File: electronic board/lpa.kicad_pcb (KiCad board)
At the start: 2 copper layers, 143 x 74 mm, 81 parts, among them CON1 BARREL_JACK, IC1 ATMEGA328-A, P2 CONN_3X2, U1 SD_CARD, U2 AP1509, U3 TLC5941, U4 TLC5941, U5 TLC5941, X1 CRYSTAL_SMD

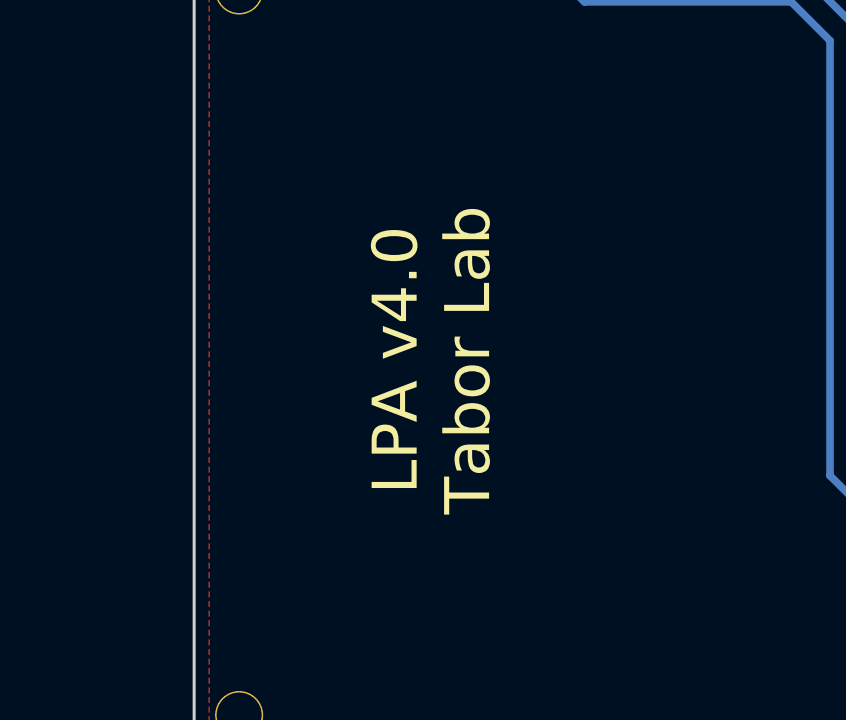
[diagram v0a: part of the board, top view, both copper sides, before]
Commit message: Updated LPA version in board silkscreen.
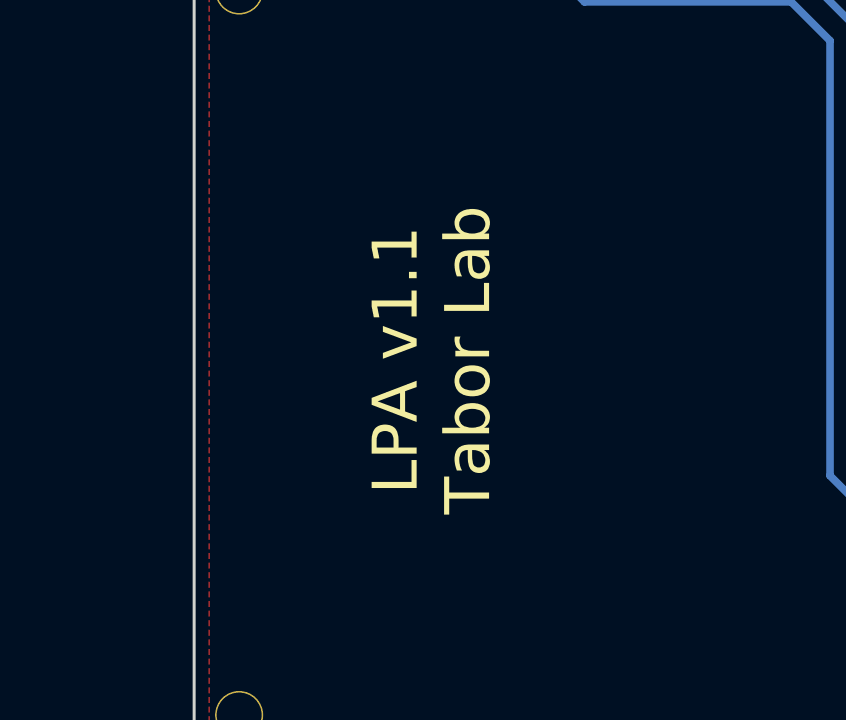
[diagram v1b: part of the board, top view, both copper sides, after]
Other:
- board text added: "LPA v1.1 Tabor Lab"
- board text removed: "LPA v4.0 Tabor Lab"
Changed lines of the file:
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@@
       (net 17 GND))
   )
-  (gr_text "LPA v4.0\nTabor Lab" (at 73.406 108.966 90) (layer F.SilkS)
+  (gr_text "LPA v1.1\nTabor Lab" (at 73.406 108.966 90) (layer F.SilkS)
     (effects (font (size 1.5 1.5) (thickness 0.3)))
   )
